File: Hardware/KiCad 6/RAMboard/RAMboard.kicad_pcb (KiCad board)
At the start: 2 copper layers, 21.6 x 38.1 mm, 4 parts, among them J1 RAMC_L, J2 RAMC_R, U1 FM18W08-SG

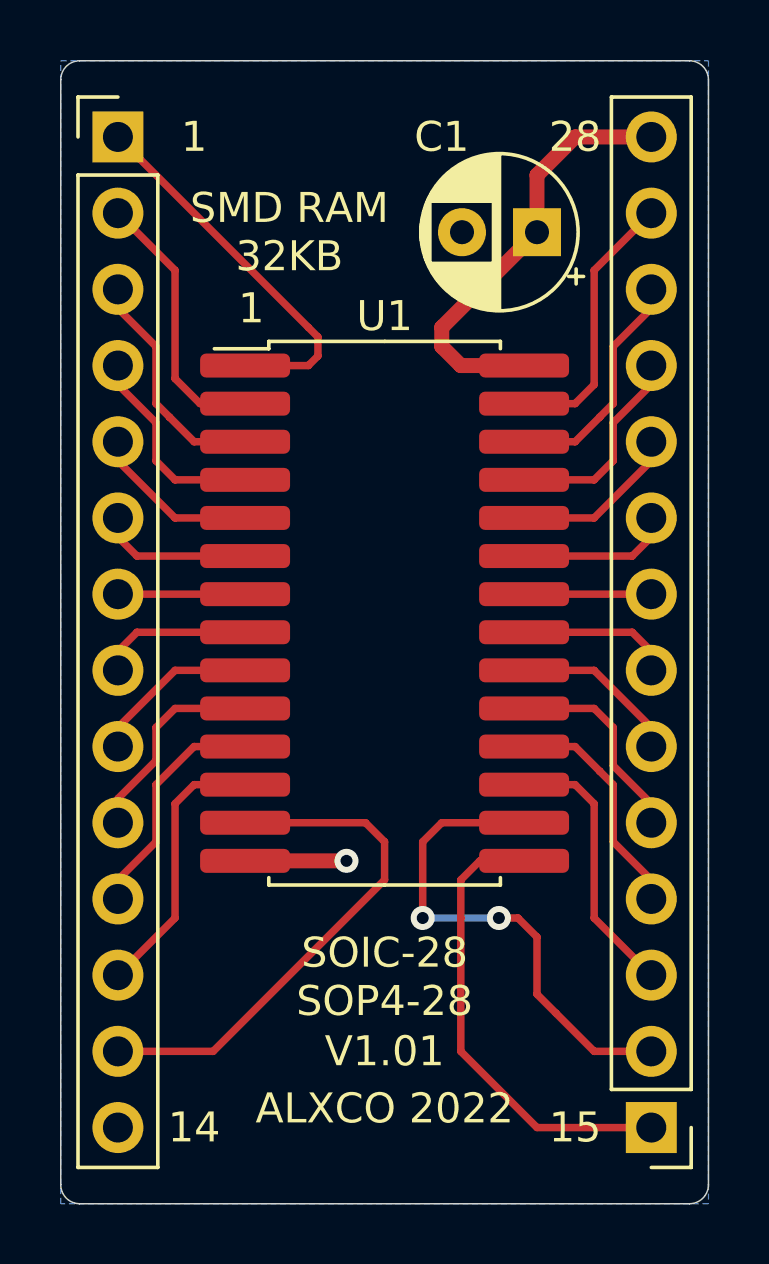
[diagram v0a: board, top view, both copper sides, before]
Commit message: Adjust orientation of RAMboard headers
Flip the pin headers to the bottom of the board, to better reflect their actual position when assembled.
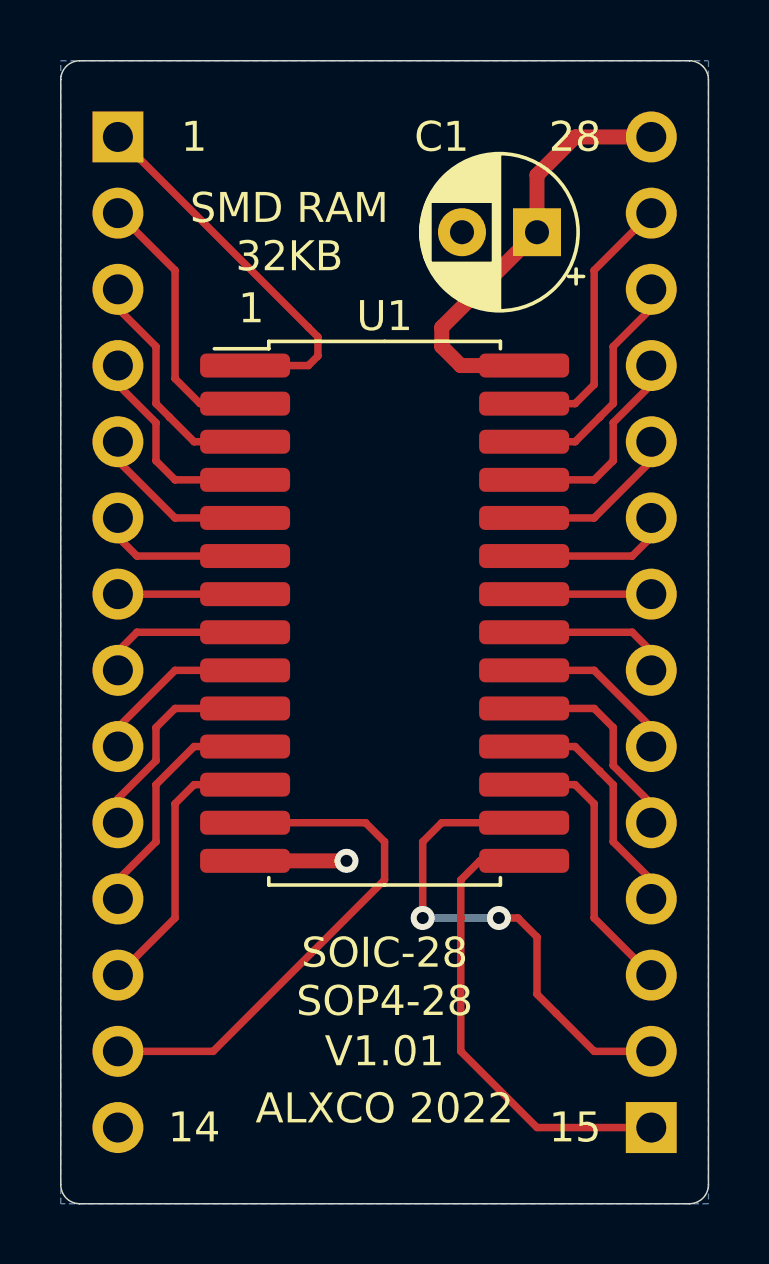
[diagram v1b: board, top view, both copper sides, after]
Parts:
- J1, J2: moved to B.Cu
- turned J1 to 180 degrees
- turned J2 to 0 degrees
